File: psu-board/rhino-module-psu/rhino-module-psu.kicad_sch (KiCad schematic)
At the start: 26 parts, among them IC1 78T

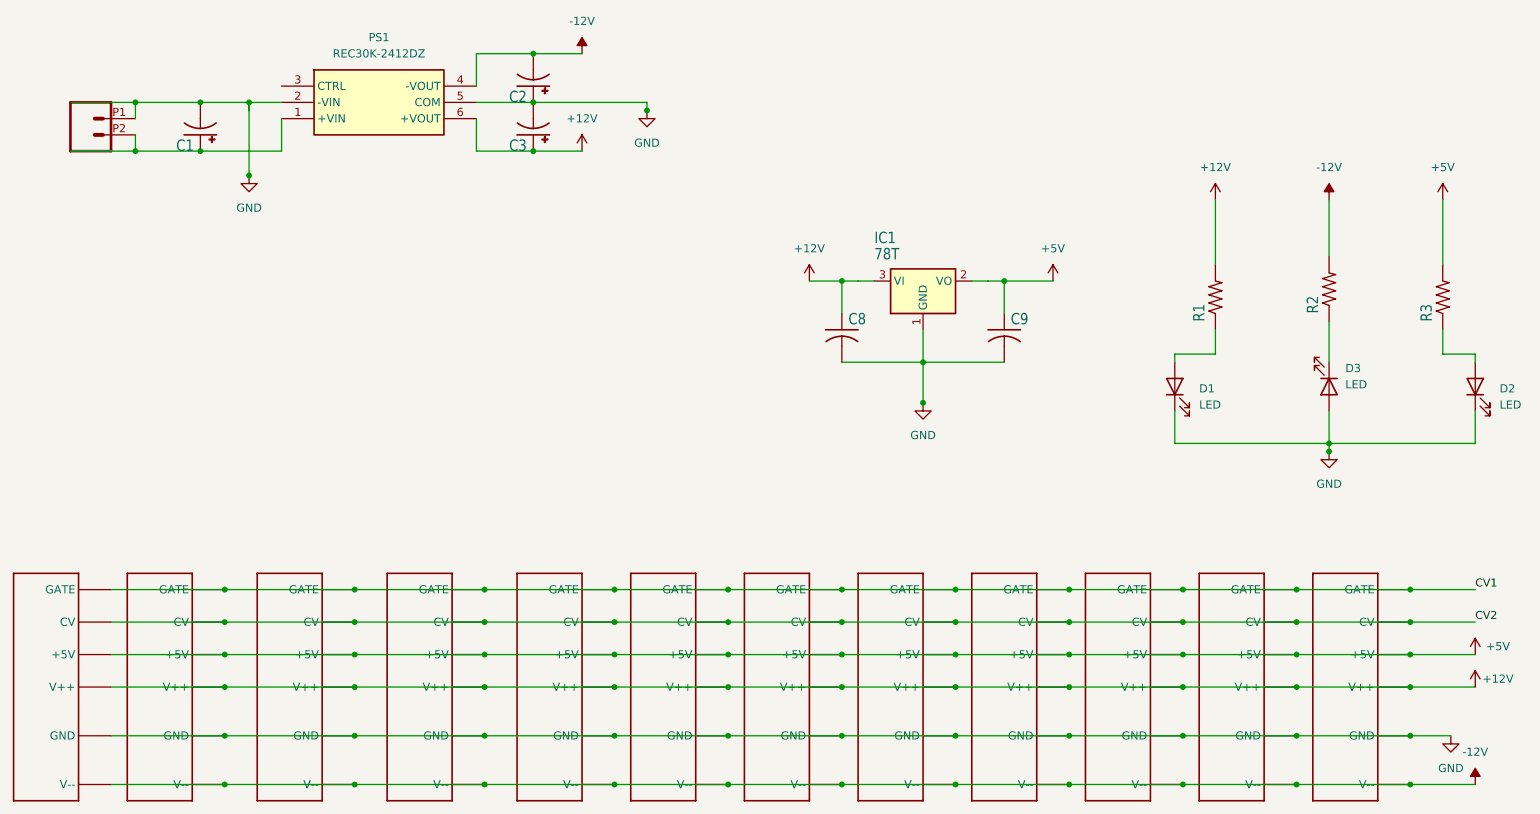
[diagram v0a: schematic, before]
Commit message: Added HSUSB datasheet
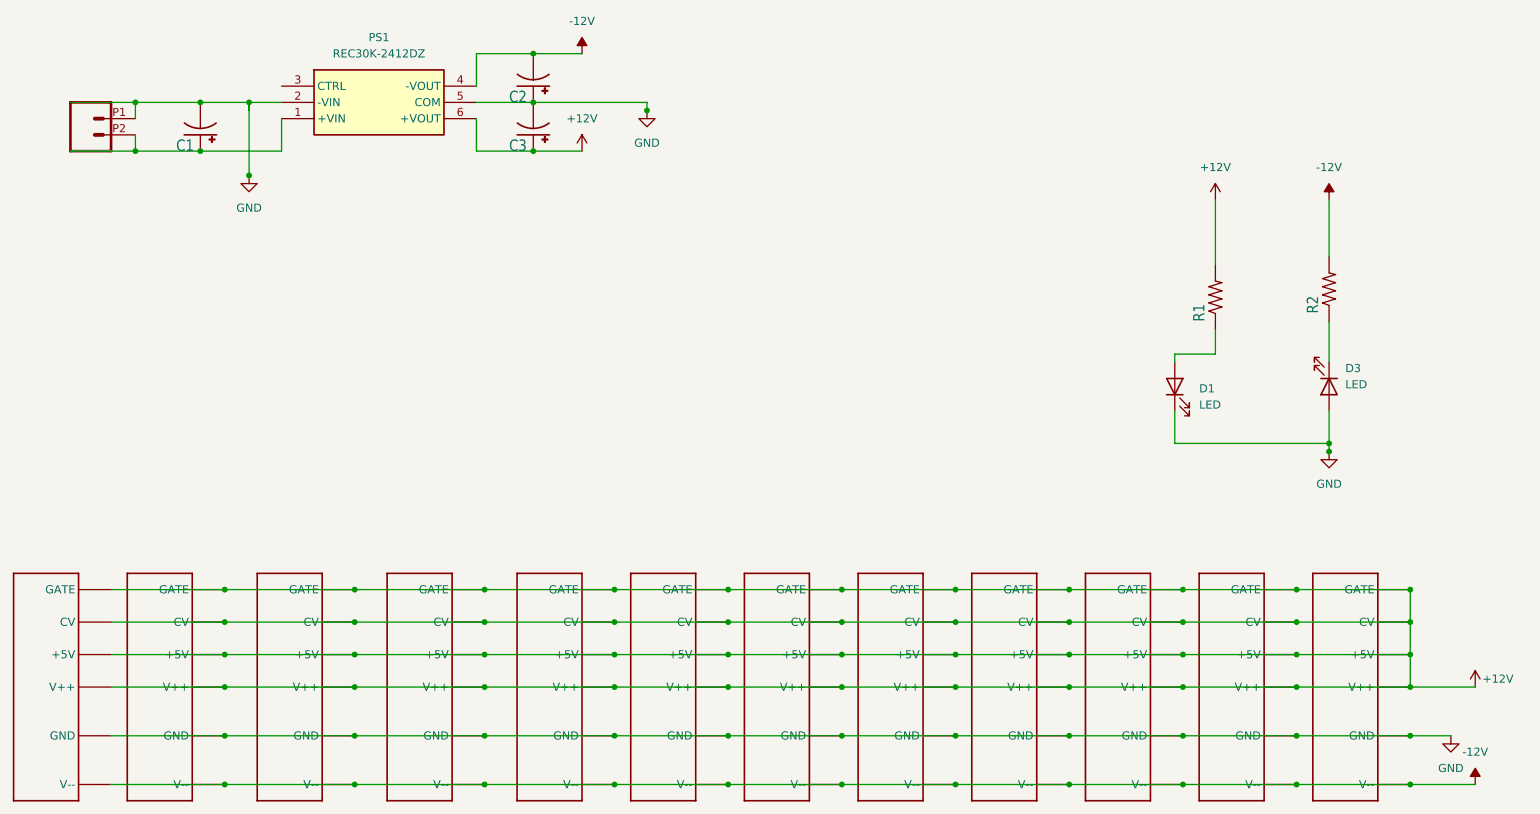
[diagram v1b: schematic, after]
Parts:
- removed C8, C9: C-US025-024X044, Capacitor_SMD:C_0603_1608Metric, symbol GMSN_Pure_Power_Strip_v1_20170629-eagle-import:C-US025-024X044
- removed D2: LED, LED_SMD:LED_0603_1608Metric, symbol Device:LED
- removed IC1: 78T, Package_TO_SOT_SMD:TO-252-3_TabPin2, symbol Regulator_Linear:LM1117DT-5.0
- removed R3: R-US_0207/10, Resistor_SMD:R_0603_1608Metric, symbol GMSN_Pure_Power_Strip_v1_20170629-eagle-import:R-US_0207/10
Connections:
- net +5V is gone; now on net +12V: U$10.+5 (+5V), U$10.+5A (+5V), U$11.+5 (+5V), U$11.+5A (+5V), U$12.+5 (+5V), U$12.+5A (+5V), U$13.+5 (+5V), U$13.+5A (+5V), U$2.+5 (+5V), U$2.+5A (+5V), U$3.+5 (+5V), U$3.+5A (+5V), U$4.+5 (+5V), U$4.+5A (+5V), U$5.+5 (+5V), U$5.+5A (+5V), U$6.+5 (+5V), U$6.+5A (+5V), U$7.+5 (+5V), U$7.+5A (+5V), U$8.+5 (+5V), U$8.+5A (+5V), U$9.+5 (+5V), U$9.+5A (+5V)
- net CV1 is gone; now on net +12V: U$10.GATE, U$10.GATEA (GATE), U$11.GATE, U$11.GATEA (GATE), U$12.GATE, U$12.GATEA (GATE), U$13.GATE, U$13.GATEA (GATE), U$2.GATE, U$2.GATEA (GATE), U$3.GATE, U$3.GATEA (GATE), U$4.GATE, U$4.GATEA (GATE), U$5.GATE, U$5.GATEA (GATE), U$6.GATE, U$6.GATEA (GATE), U$7.GATE, U$7.GATEA (GATE), U$8.GATE, U$8.GATEA (GATE), U$9.GATE, U$9.GATEA (GATE)
- net CV2 is gone; now on net +12V: U$10.CV, U$10.CVA (CV), U$11.CV, U$11.CVA (CV), U$12.CV, U$12.CVA (CV), U$13.CV, U$13.CVA (CV), U$2.CV, U$2.CVA (CV), U$3.CV, U$3.CVA (CV), U$4.CV, U$4.CVA (CV), U$5.CV, U$5.CVA (CV), U$6.CV, U$6.CVA (CV), U$7.CV, U$7.CVA (CV), U$8.CV, U$8.CVA (CV), U$9.CV, U$9.CVA (CV)
